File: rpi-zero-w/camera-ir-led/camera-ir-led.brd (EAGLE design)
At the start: 47.4 x 47.4 mm, 34 parts, among them J1 JST-PH-4

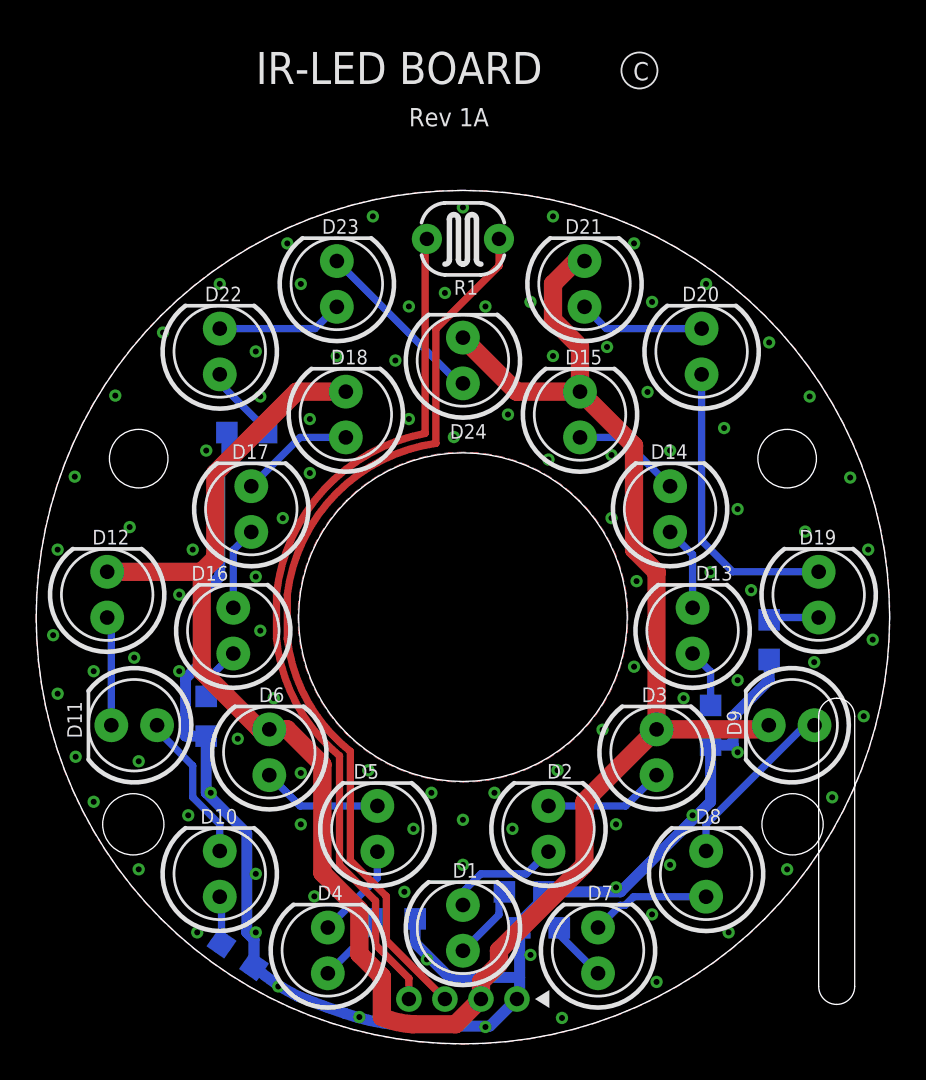
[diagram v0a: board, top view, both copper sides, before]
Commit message: moved IR LEDs
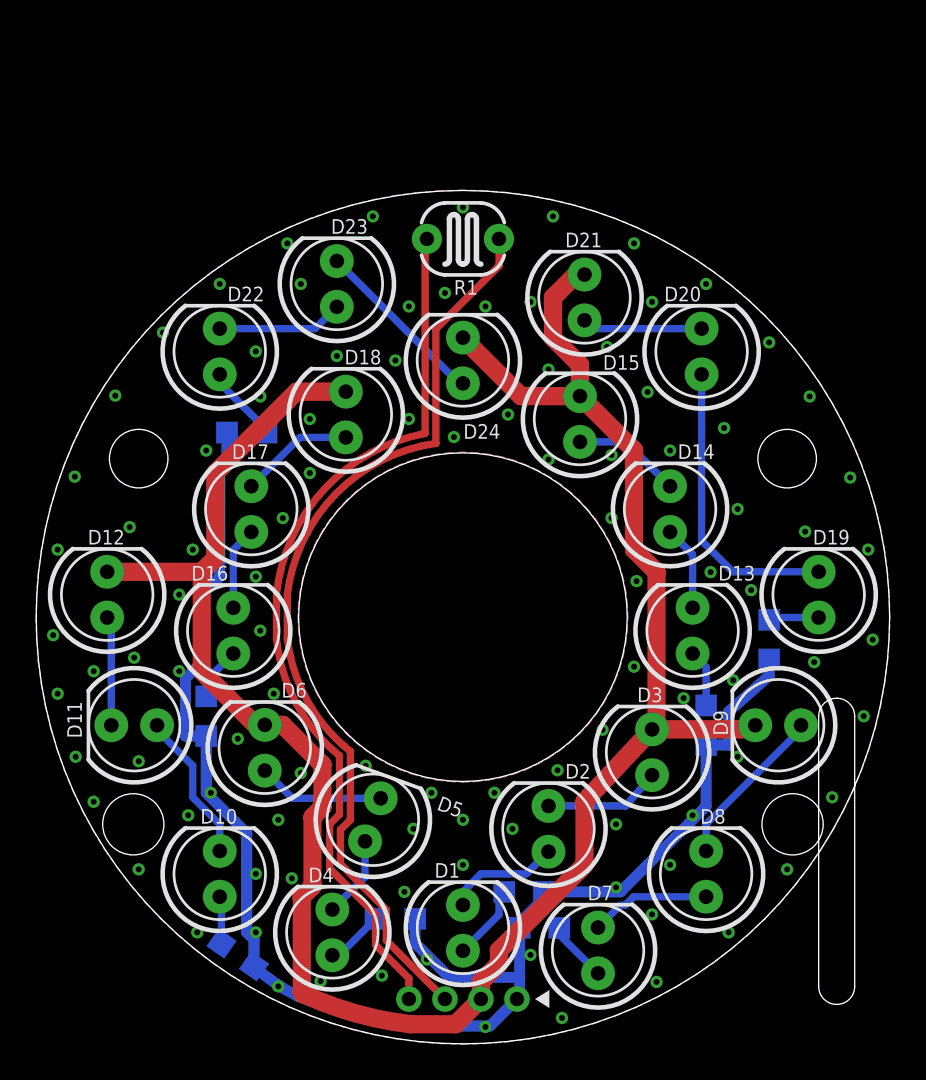
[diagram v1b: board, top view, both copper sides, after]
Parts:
- moved D4 1.03 mm to (17.0, 7.00)
- moved D21 0.75 mm to (31.0, 42.2)
- moved D9 0.75 mm to (41.8, 18.5)
- moved D5 0.56 mm to (19.2, 13.2), turned to 70 degrees
- moved D6 0.35 mm to (13.2, 17.2)
- moved D15 0.25 mm to (30.8, 35.5)
- moved D3 0.25 mm to (34.8, 17.0)
- moved R5 0.25 mm to (37.8, 18.5)
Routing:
- net GPIO18_PWM: track 118.5 -> 120.1 mm
- net N$6: track 4.12 -> 3.24 mm
- net N$5: track 5.35 -> 4.54 mm
- net N$7: track 9.78 -> 9.16 mm
- net 5V: track 84.6 -> 84.7 mm, vias 101 -> 102
